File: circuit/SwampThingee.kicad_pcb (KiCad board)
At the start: 2 copper layers, 100 x 74 mm, 89 parts, among them J2 HOLE, J3 HOLE, J4 HOLE, J5 HOLE, Q1 IRFS52N15DTRLP, Q2 BC547, SW1 reset, SW10 4S, SW2 mute, SW3 HEAD/AD, SW9 6S, U1 LM2576T-ADJ, U2 LM1117-5.0, U3 MAX6457, U4 LM1117-3.3, U5 TPA3220, U6 CSR_DebugSmall, U7 CSR8645_MODULE

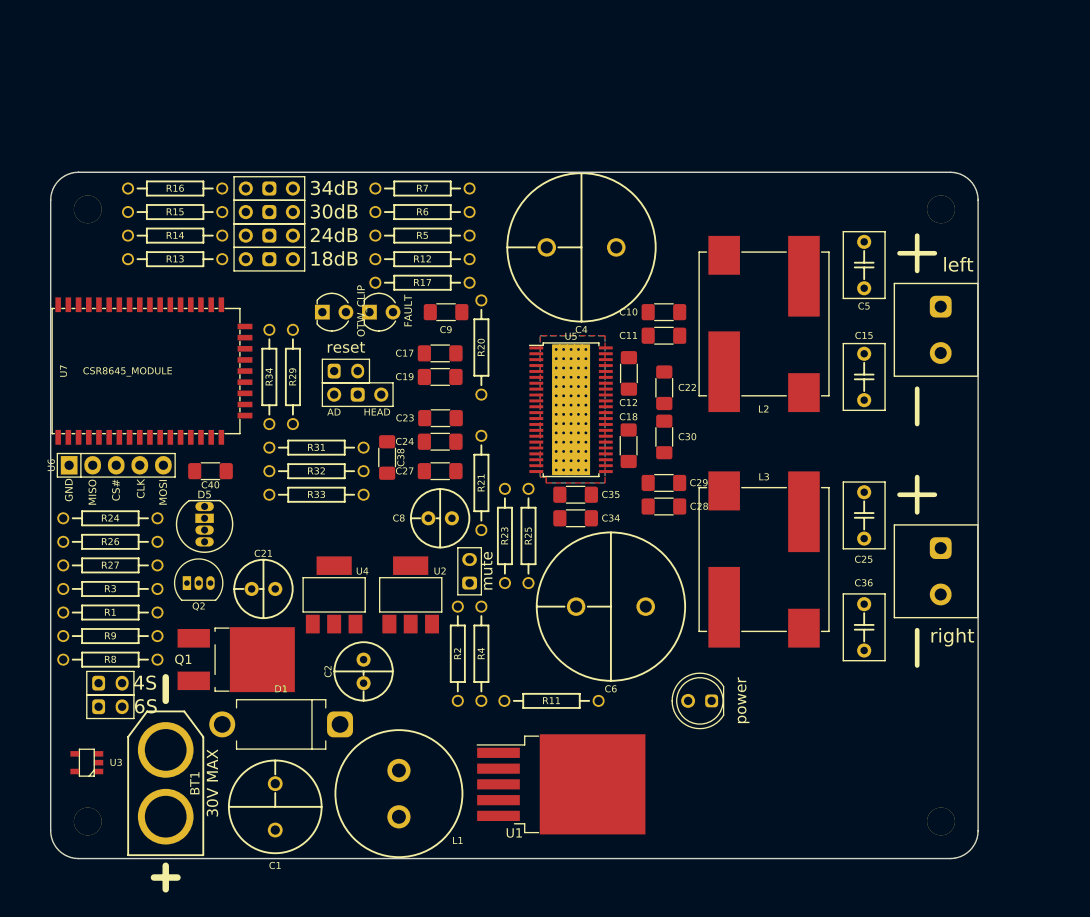
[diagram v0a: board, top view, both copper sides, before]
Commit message: squeezed swamp thingee to 100x69mm
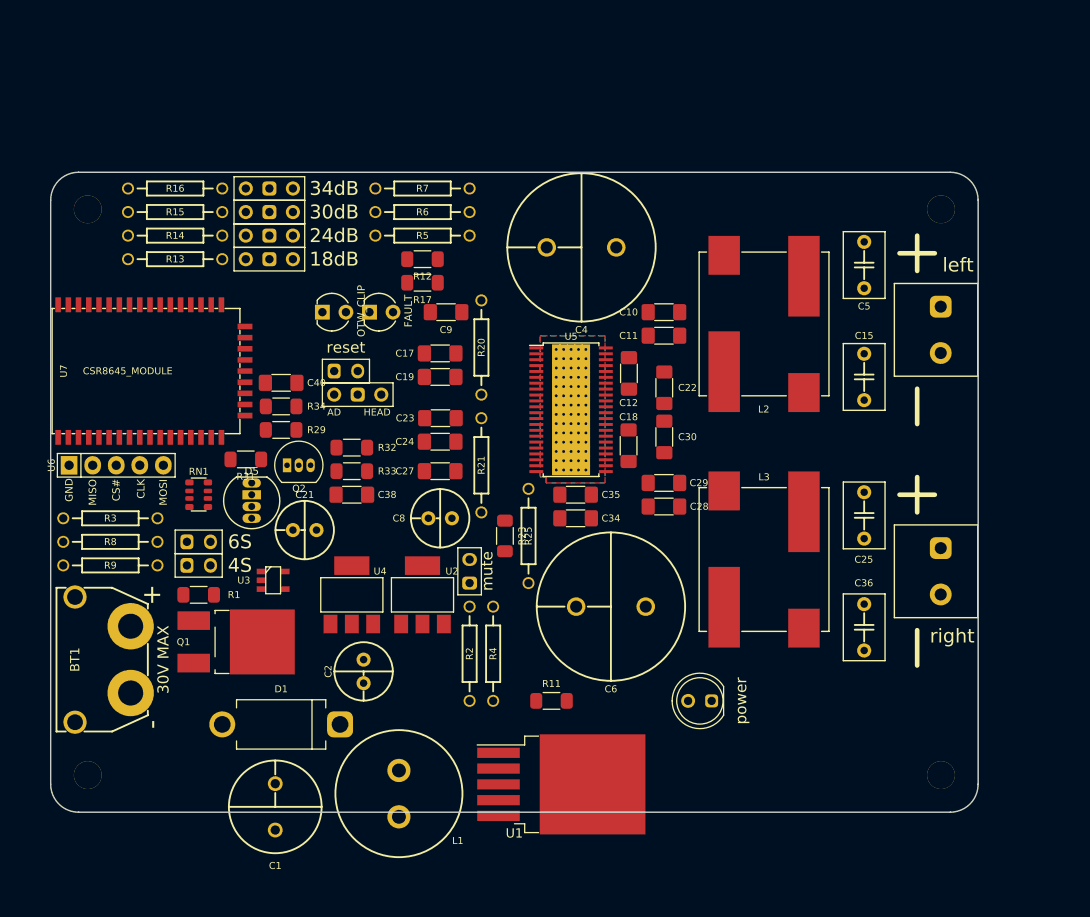
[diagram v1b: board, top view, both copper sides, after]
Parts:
- removed R24: 820, NovaBox:R_10MM
- removed R26: 220, NovaBox:R_10MM
- removed R27: 1K, NovaBox:R_10MM
- added RN1: 1K, NovaBox:Resistor_Array_x4_1206, F.Cu at (61.0, 64.8)
- BT1: footprint NovaBox:XT60-M -> NovaBox:XT60PW-M
- R1, R11, R12, R17, R23, R29, R31, R32, R33, R34: footprint NovaBox:R_10MM -> NovaBox:R_1206
- moved U3 28.1 mm to (69.0, 74.0), turned to 0 degrees
- moved SW9 20.2 mm to (61.0, 69.8)
- moved Q2 16.7 mm to (71.8, 61.6)
- moved BT1 16.5 mm to (47.6, 82.5), turned to 90 degrees
- moved SW10 15.9 mm to (61.0, 72.4)
- moved R8 12.7 mm to (51.4, 69.8), turned to 180 degrees
- moved C40 12.2 mm to (69.8, 52.7)
- moved R1 9.71 mm to (61.0, 75.6)
- moved C21 7.75 mm to (72.4, 68.6)
- moved R31 7.73 mm to (66.0, 61.0), turned to 180 degrees
- moved R3 7.62 mm to (51.4, 67.3)
- moved R9 7.62 mm to (51.4, 72.4), turned to 180 degrees
- moved R29 5.85 mm to (69.8, 57.8), turned to 0 degrees
- moved D5 5.68 mm to (66.7, 65.4)
- moved C38 5.54 mm to (77.5, 64.8), turned to 0 degrees
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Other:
- board size 100 x 74 mm -> 100 x 69 mm

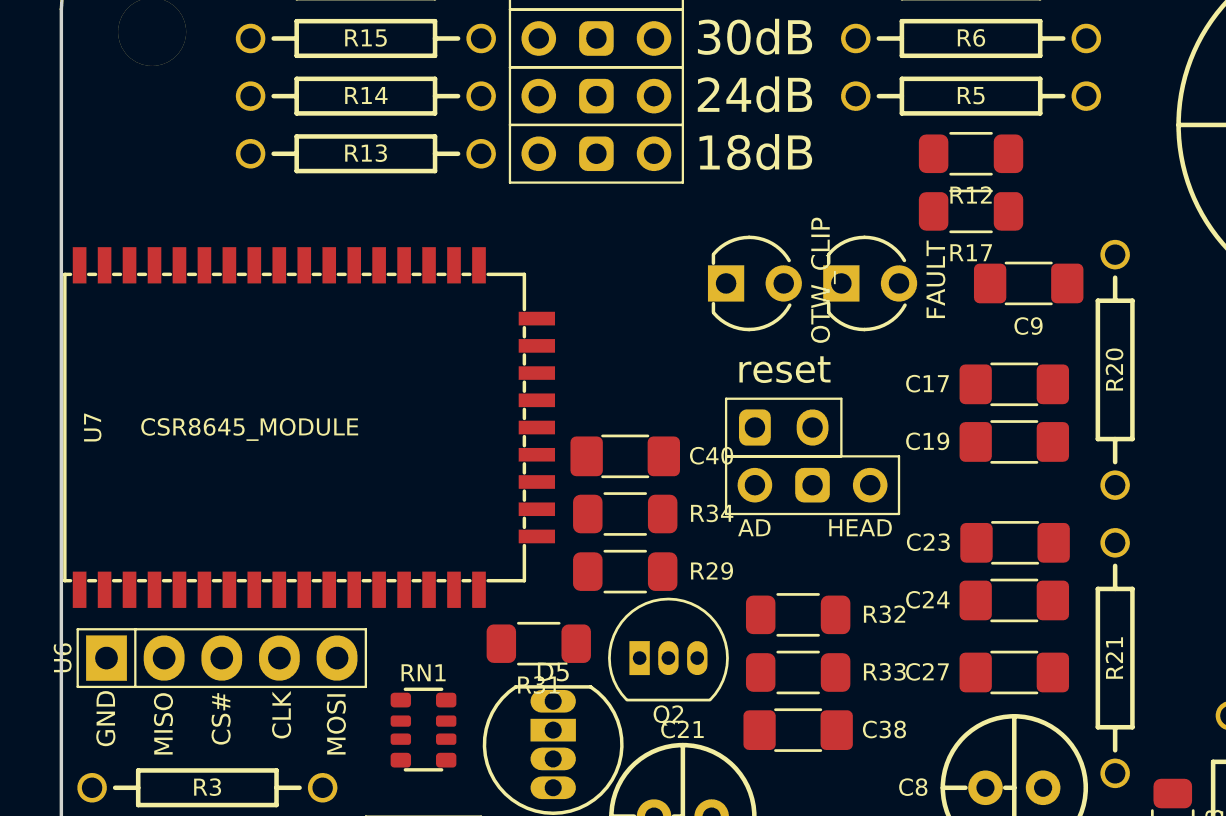
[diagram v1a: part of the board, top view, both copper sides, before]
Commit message: swamp thing assembled! TO-252 changed to TO-263
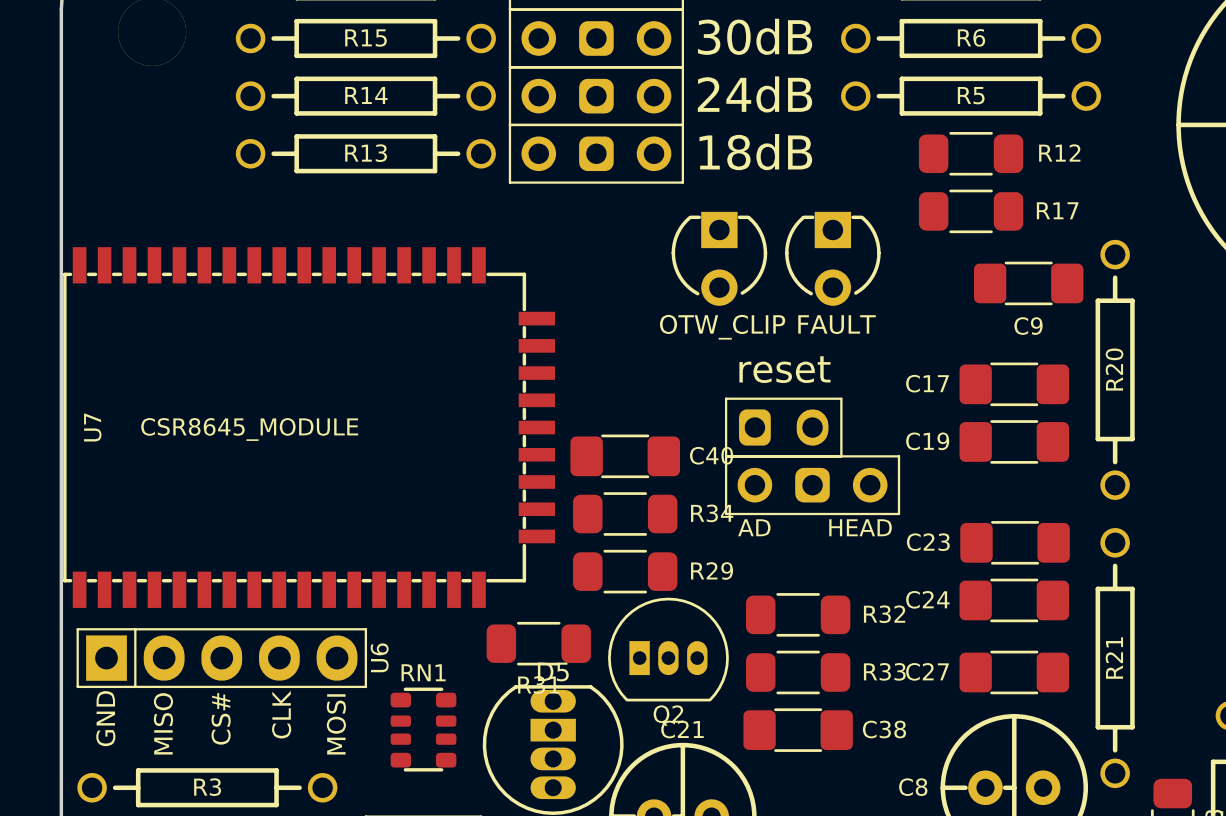
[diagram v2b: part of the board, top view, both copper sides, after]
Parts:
- moved D4 1.97 mm to (79.0, 44.0), turned to 90 degrees
- moved D2 1.90 mm to (74.0, 44.0), turned to 90 degrees
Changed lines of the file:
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@@
   (module NovaBox:CSR_DebugSmall (layer F.Cu)
     (at 52.07 61.595)
-    (fp_text reference U6 (at -6.985 0 90) (layer F.SilkS)
+    (fp_text reference U6 (at 6.985 0 90) (layer F.SilkS)
       (effects (font (size 0.762 0.762) (thickness 0.127)))
     )
@@
   )
   (module NovaBox:LED_D3.0mm (layer F.Cu)
-    (at 75.565 45.085 180)
+    (at 74 44 90)
     (descr "LED 3mm - Lead pitch 100mil (2,54mm)")
     (tags "LED led 3mm 3MM 100mil 2,54mm")
-    (fp_text reference D2 (at 0.5 -0.5 270) (layer Dwgs.User) hide
+    (fp_text reference D2 (at 0.5 -0.5 180) (layer Dwgs.User) hide
       (effects (font (size 0.0254 0.0254) (thickness 0.001)))
     )
-    (fp_text value OTW_CLIP (at -2.921 0.127 270) (layer F.SilkS)
+    (fp_text value OTW_CLIP (at -2.921 0.127 180) (layer F.SilkS)
+      (effects (font (size 0.8128 0.8128) (thickness 0.1524)))
+    )
+    (fp_arc (start 0.254 0) (end 0.254 2.032) (angle 60.2) (layer F.SilkS) (width 0.1524))
+    (fp_arc (start 0.254 0) (end 1.8034 1.31064) (angle 49.7) (layer F.SilkS) (width 0.1524))
+    (fp_arc (start 0.254 0) (end -1.5367 -0.95504) (angle 61.9) (layer F.SilkS) (width 0.1524))
+    (fp_arc (start 0.254 0) (end 0.254 -2.032) (angle 50.1) (layer F.SilkS) (width 0.1524))
+    (fp_line (start 1.8288 1.27) (end 1.8288 0.889) (layer F.SilkS) (width 0.1524))
+    (fp_line (start 1.8288 -1.27) (end 1.8288 -0.889) (layer F.SilkS) (width 0.1524))
+    (pad 1 thru_hole rect (at 1.27 0 90) (size 1.6 1.6) (drill 0.9) (layers *.Cu *.Mask)
+      (net 26 "Net-(D2-Pad1)"))
+    (pad 2 thru_hole circle (at -1.27 0 90) (size 1.6 1.6) (drill 0.9) (layers *.Cu *.Mask)
+      (net 4 +5V))
+    (model ${KISYS3DMOD}/LED_THT.3dshapes/LED_D3.0mm_Clear.wrl
+      (offset (xyz 1.25 0 -2.6))
+      (scale (xyz 1 1 1))
+      (rotate (xyz 0 0 180))
+    )
+  )
+  (module NovaBox:LED_D3.0mm (layer F.Cu)
+    (at 79 44 90)
+    (descr "LED 3mm - Lead pitch 100mil (2,54mm)")
+    (tags "LED led 3mm 3MM 100mil 2,54mm")
+    (fp_text reference D4 (at 0.5 -0.5 180) (layer Dwgs.User) hide
+      (effects (font (size 0.0254 0.0254) (thickness 0.001)))
+    )
+    (fp_text value FAULT (at -2.921 0.127 180) (layer F.SilkS)
       (effects (font (size 0.8128 0.8128) (thickness 0.1524)))
     )
@@
     (fp_arc (start 0.254 0) (end 1.8034 1.31064) (angle 49.7) (layer F.SilkS) (width 0.1524))
     (fp_arc (start 0.254 0) (end 0.254 2.032) (angle 60.2) (layer F.SilkS) (width 0.1524))
-    (pad 2 thru_hole circle (at -1.27 0 180) (size 1.6 1.6) (drill 0.9) (layers *.Cu *.Mask)
-      (net 4 +5V))
-    (pad 1 thru_hole rect (at 1.27 0 180) (size 1.6 1.6) (drill 0.9) (layers *.Cu *.Mask)
-      (net 26 "Net-(D2-Pad1)"))
-    (model ${KISYS3DMOD}/LED_THT.3dshapes/LED_D3.0mm_Clear.wrl
-      (offset (xyz 1.25 0 -2.6))
-      (scale (xyz 1 1 1))
-      (rotate (xyz 0 0 180))
-    )
-  )
-  (module NovaBox:LED_D3.0mm (layer F.Cu)
-    (at 80.645 45.085 180)
-    (descr "LED 3mm - Lead pitch 100mil (2,54mm)")
-    (tags "LED led 3mm 3MM 100mil 2,54mm")
-    (fp_text reference D4 (at 0.5 -0.5 270) (layer Dwgs.User) hide
-      (effects (font (size 0.0254 0.0254) (thickness 0.001)))
-    )
-    (fp_text value FAULT (at -2.921 0.127 270) (layer F.SilkS)
-      (effects (font (size 0.8128 0.8128) (thickness 0.1524)))
-    )
-    (fp_arc (start 0.254 0) (end 0.254 2.032) (angle 60.2) (layer F.SilkS) (width 0.1524))
-    (fp_arc (start 0.254 0) (end 1.8034 1.31064) (angle 49.7) (layer F.SilkS) (width 0.1524))
-    (fp_arc (start 0.254 0) (end -1.5367 -0.95504) (angle 61.9) (layer F.SilkS) (width 0.1524))
-    (fp_arc (start 0.254 0) (end 0.254 -2.032) (angle 50.1) (layer F.SilkS) (width 0.1524))
-    (fp_line (start 1.8288 1.27) (end 1.8288 0.889) (layer F.SilkS) (width 0.1524))
-    (fp_line (start 1.8288 -1.27) (end 1.8288 -0.889) (layer F.SilkS) (width 0.1524))
-    (pad 1 thru_hole rect (at 1.27 0 180) (size 1.6 1.6) (drill 0.9) (layers *.Cu *.Mask)
+    (pad 2 thru_hole circle (at -1.27 0 90) (size 1.6 1.6) (drill 0.9) (layers *.Cu *.Mask)
+      (net 4 +5V))
+    (pad 1 thru_hole rect (at 1.27 0 90) (size 1.6 1.6) (drill 0.9) (layers *.Cu *.Mask)
       (net 28 "Net-(D4-Pad1)"))
-    (pad 2 thru_hole circle (at -1.27 0 180) (size 1.6 1.6) (drill 0.9) (layers *.Cu *.Mask)
-      (net 4 +5V))
     (model ${KISYS3DMOD}/LED_THT.3dshapes/LED_D3.0mm_Clear.wrl
       (offset (xyz 1.25 0 -2.6))
@@
     (tags "resistor 1206")
     (attr smd)
-    (fp_text reference R12 (at 0 -1.85 180) (layer F.SilkS)
+    (fp_text reference R12 (at -3.91 0 180) (layer F.SilkS)
       (effects (font (size 0.75 0.75) (thickness 0.15)))
     )
@@
       (effects (font (size 0.0254 0.0254) (thickness 0.001)))
     )
+    (fp_line (start 0.9 0.9) (end -0.9 0.9) (layer F.SilkS) (width 0.12))
     (fp_line (start -0.9 -0.9) (end 0.9 -0.9) (layer F.SilkS) (width 0.12))
-    (fp_line (start 0.9 0.9) (end -0.9 0.9) (layer F.SilkS) (width 0.12))
+    (pad 1 smd roundrect (at -1.65 0 180) (size 1.3 1.7) (layers F.Cu F.Paste F.Mask) (roundrect_rratio 0.25)
+      (net 39 OTW_CLIP))
     (pad 2 smd roundrect (at 1.65 0 180) (size 1.3 1.7) (layers F.Cu F.Paste F.Mask) (roundrect_rratio 0.25)
       (net 26 "Net-(D2-Pad1)"))
-    (pad 1 smd roundrect (at -1.65 0 180) (size 1.3 1.7) (layers F.Cu F.Paste F.Mask) (roundrect_rratio 0.25)
-      (net 39 OTW_CLIP))
     (model Resistors_SMD.3dshapes/R_1206.wrl
       (at (xyz 0 0 0))
@@
     (tags "resistor 1206")
     (attr smd)
-    (fp_text reference R17 (at 0 -1.85 180) (layer F.SilkS)
+    (fp_text reference R17 (at -3.81 0 180) (layer F.SilkS)
       (effects (font (size 0.75 0.75) (thickness 0.15)))
     )
@@
       (effects (font (size 0.0254 0.0254) (thickness 0.001)))
     )
+    (fp_line (start -0.9 -0.9) (end 0.9 -0.9) (layer F.SilkS) (width 0.12))
     (fp_line (start 0.9 0.9) (end -0.9 0.9) (layer F.SilkS) (width 0.12))
-    (fp_line (start -0.9 -0.9) (end 0.9 -0.9) (layer F.SilkS) (width 0.12))
+    (pad 2 smd roundrect (at 1.65 0 180) (size 1.3 1.7) (layers F.Cu F.Paste F.Mask) (roundrect_rratio 0.25)
+      (net 28 "Net-(D4-Pad1)"))
     (pad 1 smd roundrect (at -1.65 0 180) (size 1.3 1.7) (layers F.Cu F.Paste F.Mask) (roundrect_rratio 0.25)
       (net 44 FAULT))
-    (pad 2 smd roundrect (at 1.65 0 180) (size 1.3 1.7) (layers F.Cu F.Paste F.Mask) (roundrect_rratio 0.25)
-      (net 28 "Net-(D4-Pad1)"))
     (model Resistors_SMD.3dshapes/R_1206.wrl
       (at (xyz 0 0 0))

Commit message: narrow swamp thingee
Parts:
- removed D1: 1N5822, NovaBox:DO-201AD_P12.70mm_Horizontal
- removed R23: 1K, NovaBox:R_1206
- removed R6: 100K, NovaBox:R_10MM
- removed S2: 18dB, NovaBox:JUMPER_3WAY
- removed S3: 24dB, NovaBox:JUMPER_3WAY
- removed S4: 30dB, NovaBox:JUMPER_3WAY
- removed S5: 34dB, NovaBox:JUMPER_3WAY
- removed SW2: mute, NovaBox:Switch_2.5mm
- added C13: 330μF, NovaBox:CPOL_D8_P3.5, F.Cu at (124.5, 43.8)
- added C14: 330μF, NovaBox:CPOL_D8_P3.5, F.Cu at (137.8, 55.9)
- added C16: 330μF, NovaBox:CPOL_D8_P3.5, F.Cu at (124.5, 85.1)
- added C20: 330μF, NovaBox:CPOL_D8_P3.5, F.Cu at (137.8, 64.1)
- added C3: 100nF, NovaBox:C_1206, F.Cu at (73.0, 104.5)
- added C7: 15μF, NovaBox:C_1812, F.Cu at (67.4, 106.8)
- added S1: GAIN_SEL, NovaBox:SR1712F-0204-20F0A-N9-N-027, F.Cu at (69.0, 24.0)
- BT1: footprint NovaBox:XT60PW-M -> NovaBox:XT60-M-NO_PM
- C1: value 100μF -> 100nF; footprint NovaBox:CPOL_D10_P4.5 -> NovaBox:C_1206
- C2: value 220μF -> 4.7μF; footprint NovaBox:CPOL_D6.3_P2.5 -> NovaBox:C_1206
- C4, C6: value 1000μF -> 330μF; footprint NovaBox:CPOL_D16_P7.5 -> NovaBox:CPOL_D8_P3.5
- D3: footprint NovaBox:LED_D5.0mm -> NovaBox:LED_D3.0mm
- L1: value 1500μH -> 68μH; footprint NovaBox:COILCRAFT_RFS1317 -> NovaBox:COIL_SRR6603
- Q1: footprint NovaBox:TO-252 -> NovaBox:TO-263-2
- R1, R11, R12, R17, R29, R31, R32, R33, R34: footprint NovaBox:R_1206 -> NovaBox:R_0805
- R13, R14, R15, R16, R20, R21, R5, R7: footprint NovaBox:R_10MM -> NovaBox:R_0805
- R2: value 7K5 -> 133K; footprint NovaBox:R_10MM -> NovaBox:R_0805
- R25: value 3R3 -> 3.3R; footprint NovaBox:R_10MM -> NovaBox:R_0805
- R3: value 16.9M -> 1.69M; footprint NovaBox:R_10MM -> NovaBox:R_0805
- R4: value 1K6 -> 22.1K; footprint NovaBox:R_10MM -> NovaBox:R_0805
- R8: value 1.05M -> 105K; footprint NovaBox:R_10MM -> NovaBox:R_0805
- R9: value 1.62M -> 162K; footprint NovaBox:R_10MM -> NovaBox:R_0805
- SPK1, SPK2: footprint NovaBox:SPKR_5MM -> NovaBox:SPKR_5MM_BLUE
- U1: value LM2576T-ADJ -> TPS560430; footprint NovaBox:TO-263-5_TabPin3 -> NovaBox:SOT-23-6
- moved C4 22.5 mm to (124.5, 34.9)
- moved C6 19.1 mm to (124.5, 76.2)
- moved C15 18.5 mm to (150.5, 57.1), turned to 0 degrees
- moved C25 18.3 mm to (150.5, 62.9), turned to 180 degrees
- moved C36 17.8 mm to (150.5, 80.0), turned to 180 degrees
- moved C5 17.8 mm to (150.5, 40.0), turned to 0 degrees
- moved L3 16.9 mm to (137.8, 77.5)
- moved L2 16.3 mm to (137.8, 42.5)
- moved C30 15.8 mm to (126.4, 62.9)
- moved C22 15.7 mm to (126.4, 57.1)
- moved C12 15.4 mm to (122.0, 56.3)
- moved C18 15.4 mm to (122.0, 63.9)
- moved C10 15.3 mm to (125.7, 49.5)
- moved C11 15.3 mm to (125.7, 52.1)
- moved C28 15.3 mm to (125.7, 70.5)
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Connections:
- C1 pad 1: +BATT -> Net-(C1-Pad1)
- C1 pad 2: GND -> Net-(C1-Pad2)
- C2 pad 1: +7.5V -> GND
- C2 pad 2: GND -> Net-(C2-Pad2)
- L1 pad 1: Net-(D1-Pad1) -> Net-(C1-Pad1)
- U1 pad 1: +BATT -> Net-(C1-Pad2)
- U1 pad 2: Net-(D1-Pad1) -> GND
- U1 pad 3: GND -> Net-(R2-Pad2)
- U1 pad 4: Net-(R2-Pad2) -> Net-(C2-Pad2)
- U1 pad 5: GND -> Net-(C2-Pad2)
- U5 pad 2: Net-(S2-Pad2) -> /GAIN_SLV
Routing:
- removed copper zone on B.Cu, net GND
- removed copper zone on F.Cu, net GND
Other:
- board size 100 x 69 mm -> 110 x 60 mm

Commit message: swamp thingee continued
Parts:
- removed R11: 10K, NovaBox:R_0805
- added J1: USB_OTG, NovaBox:USB_MiniB_THT, F.Cu at (48.3, 36.2)
- added R6: 10K, NovaBox:R_0805, F.Cu at (98.4, 82.5)
- BT1: value 30V MAX -> 28V MAX
- D5: footprint NovaBox:LED_RABG -> NovaBox:LED_D5.0mm_RGB
- moved C7 55.3 mm to (114.3, 77.5)
- moved D2 43.8 mm to (116.8, 34.9), turned to 270 degrees
- moved C3 43.6 mm to (112.4, 85.7), turned to 180 degrees
- moved C1 40.7 mm to (106.7, 82.5), turned to 180 degrees
- moved D4 38.5 mm to (117.5, 45.7), turned to 270 degrees
- moved S1 35.7 mm to (101.0, 40.0), turned to 90 degrees
- moved R7 32.9 mm to (113.0, 42.5), turned to 270 degrees
- moved R17 31.1 mm to (117.5, 49.5), turned to 0 degrees
- moved R12 30.5 mm to (117.5, 38.7), turned to 0 degrees
- moved R8 30.0 mm to (76.2, 78.1)
- moved R9 29.7 mm to (76.2, 80.0)
- moved R13 29.2 mm to (87.6, 38.1)
- moved R14 29.2 mm to (87.6, 36.2)
- moved R16 29.2 mm to (87.6, 32.4)
- moved R15 29.2 mm to (87.6, 34.3)
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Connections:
- C2 pad 2: Net-(C2-Pad2) -> +BATT
- C3 pad 2: Net-(C2-Pad2) -> +BATT
- U1 pad 4: Net-(C2-Pad2) -> +BATT
- U1 pad 5: Net-(C2-Pad2) -> +BATT
- U7 pad 12: (no net) -> VBUS
- U7 pad 24: (no net) -> /USB_D-
- U7 pad 25: (no net) -> /USB_D+
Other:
- board size 110 x 60 mm -> 100 x 60 mm

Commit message: swamp thingee laid out
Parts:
- D2, D4: footprint NovaBox:LED_D3.0mm -> NovaBox:LED_D5.0mm
- D3: value power -> POWER; footprint NovaBox:LED_D3.0mm -> NovaBox:LED_D5.0mm
- J1: value USB_OTG -> CONN_01X04; footprint NovaBox:USB_MiniB_THT -> NovaBox:PIN_1x4_P2.00mm
- R13: value 5K6 -> 5.6K
- SW1: value reset -> RESET
- moved J1 34.1 mm to (80.6, 47.0), turned to 270 degrees
- moved R6 15.2 mm to (83.2, 82.5), turned to 180 degrees
- moved R1 12.7 mm to (83.2, 80.6), turned to 0 degrees
- moved C1 11.1 mm to (97.2, 76.8)
- moved R2 11.1 mm to (93.3, 80.0)
- moved R4 11.1 mm to (91.4, 80.0)
- moved U1 11.1 mm to (97.2, 80.0)
- moved D3 11.1 mm to (88.3, 83.8)
- moved C2 10.5 mm to (102.9, 83.8)
- moved L1 10.5 mm to (104.8, 77.5)
- moved C3 10.5 mm to (102.9, 81.3)
- moved C8 8.54 mm to (91.4, 61.6)
- moved R17 8.28 mm to (116.8, 41.3)
- moved R8 7.10 mm to (83.2, 76.8)
- moved R9 7.10 mm to (83.2, 78.7)
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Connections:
- net Net-(R34-Pad2) renamed /RST
- net Net-(RN1-Pad5) renamed /RED
- net Net-(RN1-Pad6) renamed /GRN
- net Net-(RN1-Pad8) renamed /BLU
- net Net-(U6-Pad1) renamed /MOSI
- net Net-(U6-Pad2) renamed /CLK
- net Net-(U6-Pad3) renamed /CS#
- net Net-(U6-Pad4) renamed /MISO
- J1 pad 2: /USB_D- -> /USB_D+
- J1 pad 3: /USB_D+ -> /USB_D-
- J1 pad 4: (no net) -> GND
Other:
- board text added: "D+"
- board text added: "D-"
- board text added: "GND"
- board text added: "VBUS"
